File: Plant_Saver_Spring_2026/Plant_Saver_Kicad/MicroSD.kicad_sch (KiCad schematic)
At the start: 7 parts, among them J3 DM3D-SF

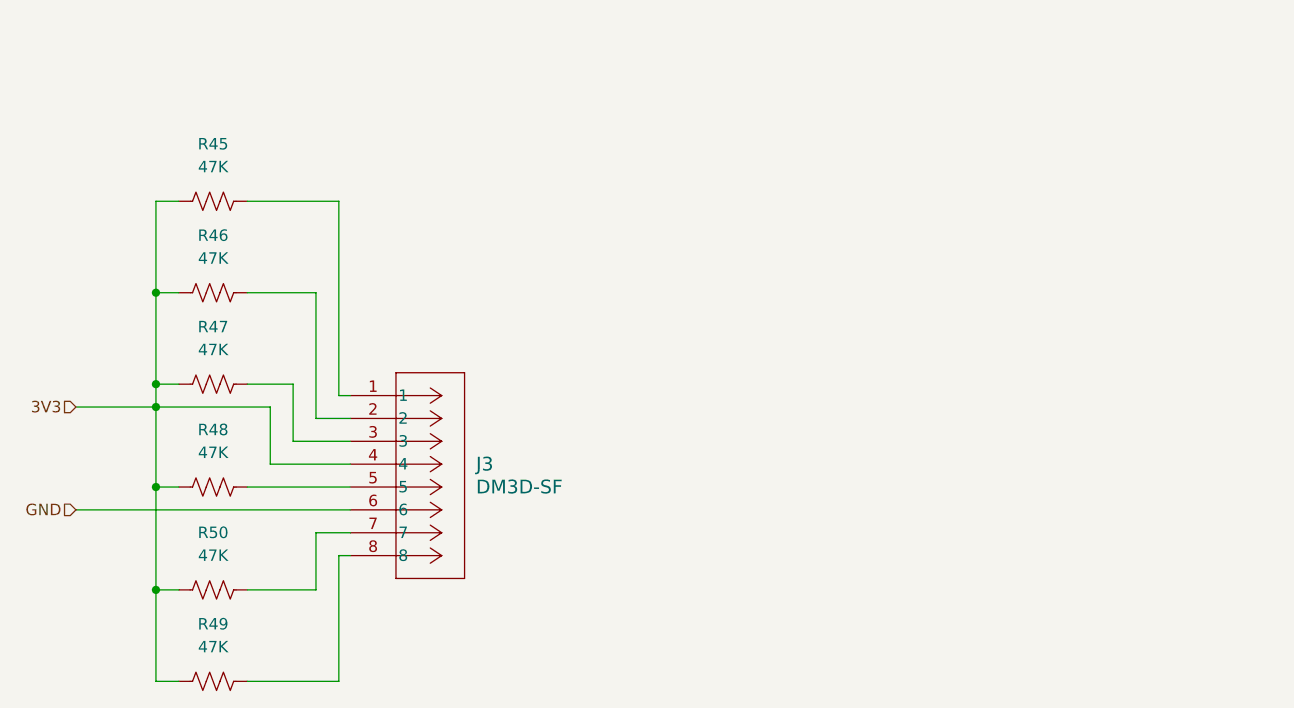
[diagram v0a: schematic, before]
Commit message: Micro-SD subsheet
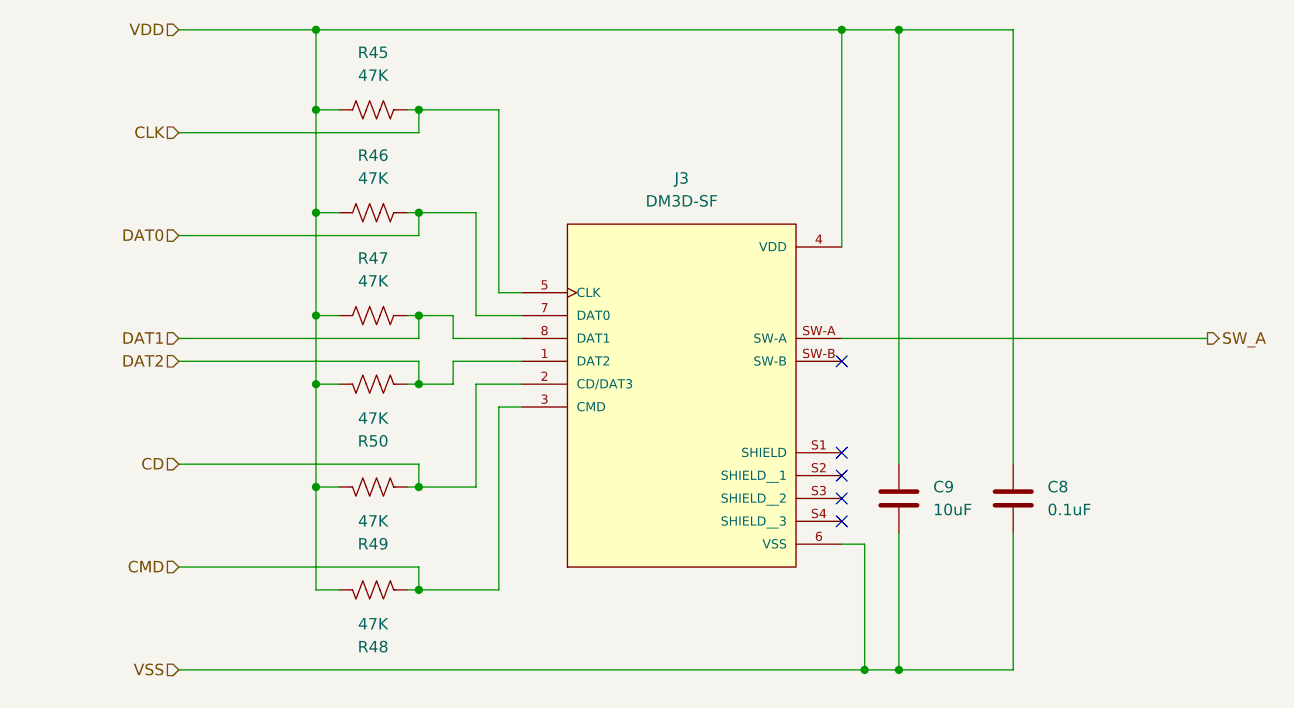
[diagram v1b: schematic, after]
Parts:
- added C8: 0.1uF, Capacitor_SMD:C_1206_3216Metric_Pad1.33x1.80mm_HandSolder, symbol Device:C
- added C9: 10uF, Capacitor_SMD:C_1206_3216Metric_Pad1.33x1.80mm_HandSolder, symbol Device:C
- J3: footprint DM3D_SF:CONN8_DM3D-SF_HIR -> DM3D_SF:HRS_DM3D-SF; MANUFACTURER (none) -> Hirose; MAXIMUM_PACKAGE_HEIGHT (none) -> 1.55mm; PARTREV (none) -> 2017.1; STANDARD (none) -> Manufacturer Recommendations
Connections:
- net CLK: now reaches J3.5 (CLK)
- net CLK: now also R45.2; no longer R48.2
- net DAT0: now reaches J3.7 (DAT0)
- net DAT0: now also R46.2; no longer R50.2
- net DAT2: now reaches J3.1 (DAT2)
- net DAT2: now also R50.2; no longer R45.2
- net CD: now reaches J3.2 (CD/DAT3)
- net CD: now also R49.2; no longer R46.2
- net CMD: now reaches J3.3 (CMD)
- net CMD: now also R48.2; no longer R47.2
- net DAT1: now reaches J3.8 (DAT1)
- net DAT1: now also R47.2; no longer R49.2
- net 3V3 renamed VDD
- net VDD: now also C8.1, C9.1
- net GND renamed VSS
- net VSS: now also C8.2, C9.2
- new net SW_A: J3.SW-A
- no-connect marks 0 -> 5
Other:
- moved on the sheet: R45, R46, R47

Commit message: Misc. changes
Updated peripheral power switch, UI board connections
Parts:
- R45, R46, R47, R48, R49, R50: value 47K -> 10K
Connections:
- net VDD is gone; now on net CD: C8.1, C9.1, J3.4 (VDD), R45.1, R46.1, R47.1, R48.1, R49.1, R50.1
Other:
- moved on the sheet: R48, R49, R50

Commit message: Started PCB
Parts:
- renumbered C8 to C10, J3 to J10, R45 to R18, R46 to R19, R47 to R20, R50 to R21, R49 to R22, R48 to R23
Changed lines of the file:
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@@
 		(dnp no)
 		(fields_autoplaced yes)
-		(property "Reference" "R48"
+		(property "Reference" "R23"
 			(at 116.84 109.22 90)
 			(effects
@@
 			(project "Plant_Saver_Kicad"
 				(path "/7f244634-d37a-4ff0-ba36-8027330ab1bd/bf3b52d9-1787-462a-86c6-de9a695c648b"
-					(reference "R48")
+					(reference "R23")
 					(unit 1)
 				)
@@
 		(dnp no)
 		(fields_autoplaced yes)
-		(property "Reference" "R50"
+		(property "Reference" "R21"
 			(at 116.84 88.9 90)
 			(effects
@@
 			(project "Plant_Saver_Kicad"
 				(path "/7f244634-d37a-4ff0-ba36-8027330ab1bd/bf3b52d9-1787-462a-86c6-de9a695c648b"
-					(reference "R50")
+					(reference "R21")
 					(unit 1)
 				)
@@
 		(dnp no)
 		(fields_autoplaced yes)
-		(property "Reference" "R47"
+		(property "Reference" "R20"
 			(at 116.84 77.47 90)
 			(effects
@@
 			(project "Plant_Saver_Kicad"
 				(path "/7f244634-d37a-4ff0-ba36-8027330ab1bd/bf3b52d9-1787-462a-86c6-de9a695c648b"
-					(reference "R47")
+					(reference "R20")
 					(unit 1)
 				)
@@
 		(dnp no)
 		(fields_autoplaced yes)
-		(property "Reference" "R45"
+		(property "Reference" "R18"
 			(at 116.84 54.61 90)
 			(effects
@@
 			(project ""
 				(path "/7f244634-d37a-4ff0-ba36-8027330ab1bd/bf3b52d9-1787-462a-86c6-de9a695c648b"
-					(reference "R45")
+					(reference "R18")
 					(unit 1)
 				)
@@
 		(dnp no)
 		(fields_autoplaced yes)
-		(property "Reference" "J3"
+		(property "Reference" "J10"
 			(at 151.13 68.58 0)
 			(effects
@@
 			(project ""
 				(path "/7f244634-d37a-4ff0-ba36-8027330ab1bd/bf3b52d9-1787-462a-86c6-de9a695c648b"
-					(reference "J3")
+					(reference "J10")
 					(unit 1)
 				)
@@
 		(dnp no)
 		(fields_autoplaced yes)
-		(property "Reference" "C8"
+		(property "Reference" "C10"
 			(at 191.77 102.8699 0)
 			(effects
@@
 			(project ""
 				(path "/7f244634-d37a-4ff0-ba36-8027330ab1bd/bf3b52d9-1787-462a-86c6-de9a695c648b"
-					(reference "C8")
+					(reference "C10")
 					(unit 1)
 				)
@@
 		(dnp no)
 		(fields_autoplaced yes)
-		(property "Reference" "R46"
+		(property "Reference" "R19"
 			(at 116.84 66.04 90)
 			(effects
@@
 			(project "Plant_Saver_Kicad"
 				(path "/7f244634-d37a-4ff0-ba36-8027330ab1bd/bf3b52d9-1787-462a-86c6-de9a695c648b"
-					(reference "R46")
+					(reference "R19")
 					(unit 1)
 				)
@@
 		(dnp no)
 		(fields_autoplaced yes)
-		(property "Reference" "R49"
+		(property "Reference" "R22"
 			(at 116.84 99.06 90)
 			(effects
@@
 			(project "Plant_Saver_Kicad"
 				(path "/7f244634-d37a-4ff0-ba36-8027330ab1bd/bf3b52d9-1787-462a-86c6-de9a695c648b"
-					(reference "R49")
-					(unit 1)
-				)
+					(reference "R22")
+					(unit 1)
+				)

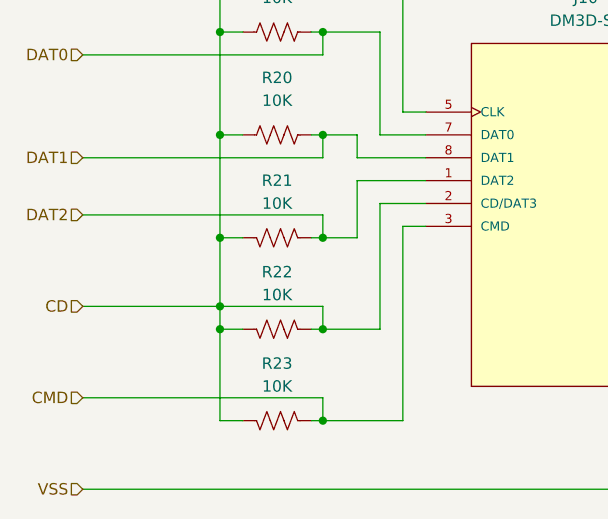
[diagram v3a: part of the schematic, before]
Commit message: Refined PCB layout
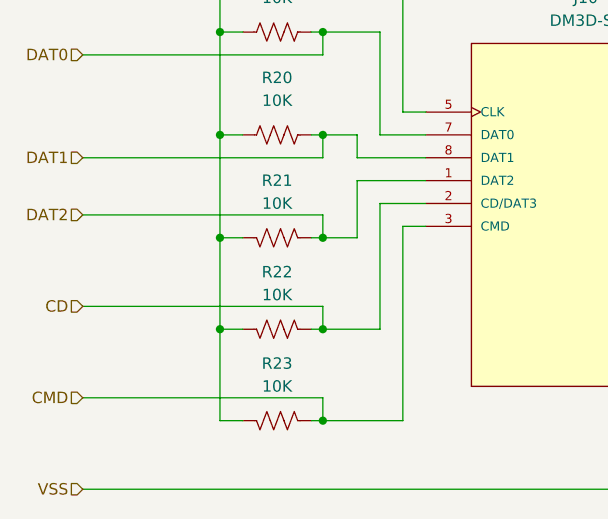
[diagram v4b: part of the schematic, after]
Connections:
- net CD: no longer C10.1, C9.1, J10.4 (VDD), R18.1, R19.1, R20.1, R21.1, R22.1, R23.1
- new net VDD: C10.1, C9.1, J10.4 (VDD), R18.1, R19.1, R20.1, R21.1, R22.1, R23.1
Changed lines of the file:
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@@
-	)
-	(junction
-		(at 110.49 102.87)
-		(diameter 0)
-		(color 0 0 0 0)
 	)
 	(junction
@@
 	(wire
 		(pts
-			(xy 95.25 102.87) (xy 110.49 102.87)
-		)
-		(stroke
-			(width 0)
-			(type default)
-		)
-	)
-	(wire
-		(pts
 			(xy 120.65 83.82) (xy 121.92 83.82)
 		)
@@
 	(wire
 		(pts
-			(xy 110.49 95.25) (xy 110.49 102.87)
-		)
-		(stroke
-			(width 0)
-			(type default)
-		)
-	)
-	(wire
-		(pts
 			(xy 121.92 105.41) (xy 121.92 102.87)
 		)
@@
 	(wire
 		(pts
-			(xy 110.49 105.41) (xy 110.49 102.87)
+			(xy 110.49 95.25) (xy 110.49 105.41)
 		)
 		(stroke
@@
 	(wire
 		(pts
-			(xy 110.49 102.87) (xy 121.92 102.87)
-		)
-		(stroke
+			(xy 95.25 102.87) (xy 121.92 102.87)
+		)
+		(stroke

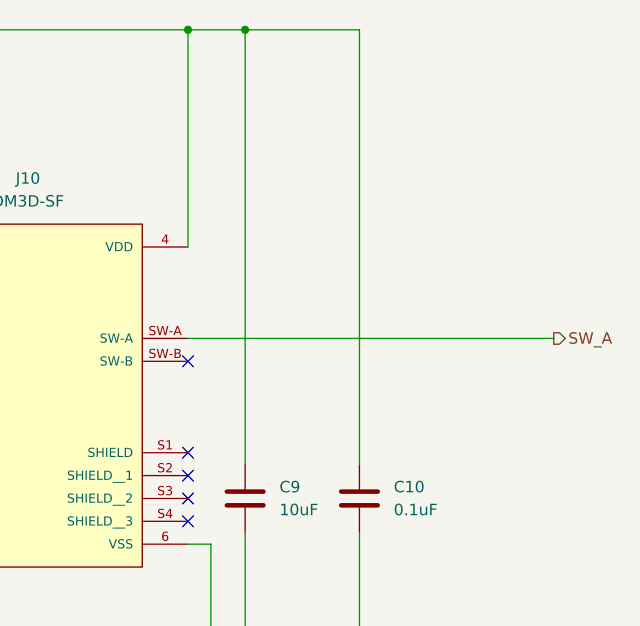
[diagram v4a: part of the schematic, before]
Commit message: Nearly finished routing
uSD and two I2C connectors remaining.
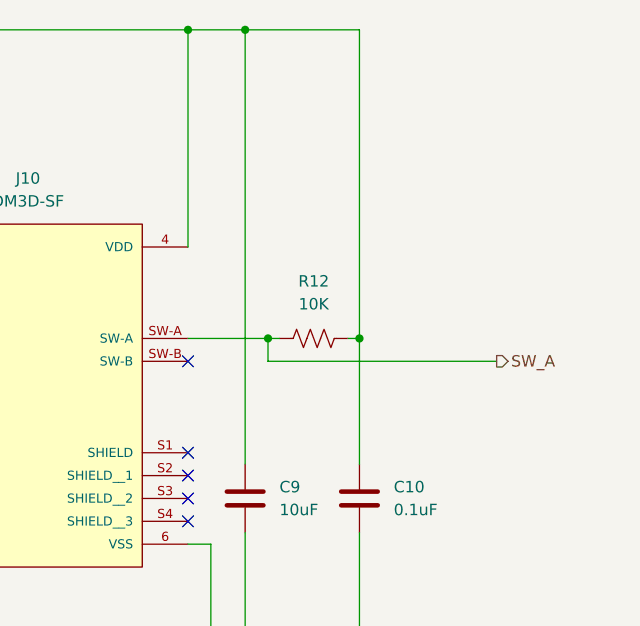
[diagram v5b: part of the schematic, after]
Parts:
- added R12: 10K, Resistor_SMD:R_1206_3216Metric_Pad1.30x1.75mm_HandSolder, symbol Device:R_US
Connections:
- net SW_A: now also R12.1
- net VDD: now also R12.2
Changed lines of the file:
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@@
+	)
+	(junction
+		(at 177.8 86.36)
+		(diameter 0)
+		(color 0 0 0 0)
 	)
 	(junction
@@
 	)
 	(junction
+		(at 187.96 86.36)
+		(diameter 0)
+		(color 0 0 0 0)
+	)
+	(junction
 		(at 110.49 72.39)
 		(diameter 0)
@@
 	(wire
 		(pts
+			(xy 177.8 88.9) (xy 177.8 86.36)
+		)
+		(stroke
+			(width 0)
+			(type default)
+		)
+	)
+	(wire
+		(pts
 			(xy 120.65 95.25) (xy 121.92 95.25)
 		)
@@
 	(wire
 		(pts
+			(xy 186.69 86.36) (xy 187.96 86.36)
+		)
+		(stroke
+			(width 0)
+			(type default)
+		)
+	)
+	(wire
+		(pts
 			(xy 125.73 86.36) (xy 133.35 86.36)
 		)
@@
 	(wire
 		(pts
-			(xy 168.91 86.36) (xy 209.55 86.36)
-		)
-		(stroke
-			(width 0)
-			(type default)
-		)
-	)
-	(wire
-		(pts
 			(xy 128.27 72.39) (xy 128.27 83.82)
 		)
@@
 	(wire
 		(pts
+			(xy 203.2 88.9) (xy 177.8 88.9)
+		)
+		(stroke
+			(width 0)
+			(type default)
+		)
+	)
+	(wire
+		(pts
 			(xy 175.26 123.19) (xy 171.45 123.19)
 		)
@@
 	(wire
 		(pts
+			(xy 187.96 86.36) (xy 187.96 100.33)
+		)
+		(stroke
+			(width 0)
+			(type default)
+		)
+	)
+	(wire
+		(pts
 			(xy 95.25 102.87) (xy 121.92 102.87)
 		)
@@
 	(wire
 		(pts
+			(xy 168.91 86.36) (xy 177.8 86.36)
+		)
+		(stroke
+			(width 0)
+			(type default)
+		)
+	)
+	(wire
+		(pts
 			(xy 110.49 60.96) (xy 110.49 72.39)
 		)
@@
 	(wire
 		(pts
-			(xy 187.96 52.07) (xy 187.96 100.33)
+			(xy 187.96 52.07) (xy 187.96 86.36)
 		)
 		(stroke
@@
 		(pts
 			(xy 121.92 115.57) (xy 130.81 115.57)
+		)
+		(stroke
+			(width 0)
+			(type default)
+		)
+	)
+	(wire
+		(pts
+			(xy 177.8 86.36) (xy 179.07 86.36)
 		)
 		(stroke
@@
 	(hierarchical_label "SW_A"
 		(shape output)
-		(at 209.55 86.36 0)
+		(at 203.2 88.9 0)
 		(effects
 			(font
@@
 					(unit 1)
 				)
+			)
+		)
+	)
+	(symbol
+		(lib_id "Device:R_US")
+		(at 182.88 86.36 90)
+		(unit 1)
+		(exclude_from_sim no)
+		(in_bom yes)
+		(on_board yes)
+		(dnp no)
+		(property "Reference" "R12"
+			(at 182.88 80.01 90)
+			(effects
+				(font
+					(size 1.27 1.27)
+				)
+			)
+		)
+		(property "Value" "10K"
+			(at 182.88 82.55 90)
+			(effects
+				(font
+					(size 1.27 1.27)
+				)
+			)
+		)
+		(property "Footprint" "Resistor_SMD:R_1206_3216Metric_Pad1.30x1.75mm_HandSolder"
+			(at 183.134 85.344 90)
+			(effects
+				(font
+					(size 1.27 1.27)
+				)
+				(hide yes)
+			)
+		)
+		(property "Datasheet" "~"
+			(at 182.88 86.36 0)
+			(effects
+				(font
+					(size 1.27 1.27)
+				)
+				(hide yes)
+			)
+		)
+		(property "Description" "Resistor, US symbol"
+			(at 182.88 86.36 0)
+			(effects
+				(font
+					(size 1.27 1.27)
+				)
+				(hide yes)
+			)
+		)
+		(pin "1"
+		)
+		(pin "2"
+		)
+		(instances
+			(project "Plant_Saver_Kicad"
+				(path "/7f244634-d37a-4ff0-ba36-8027330ab1bd/bf3b52d9-1787-462a-86c6-de9a695c648b"
+					(reference "R12")
+					(unit 1)
+				)

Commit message: PCB Pre-Check complete
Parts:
- renumbered J10 to J11, R18 to R19, R19 to R20, R20 to R21, R21 to R22, R22 to R23, R23 to R24, R12 to R25
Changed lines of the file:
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@@
 		(dnp no)
 		(fields_autoplaced yes)
-		(property "Reference" "R23"
+		(property "Reference" "R24"
 			(at 116.84 109.22 90)
 			(effects
@@
 			(project "Plant_Saver_Kicad"
 				(path "/7f244634-d37a-4ff0-ba36-8027330ab1bd/bf3b52d9-1787-462a-86c6-de9a695c648b"
-					(reference "R23")
+					(reference "R24")
 					(unit 1)
 				)
@@
 		(dnp no)
 		(fields_autoplaced yes)
-		(property "Reference" "R21"
+		(property "Reference" "R22"
 			(at 116.84 88.9 90)
 			(effects
@@
 			(project "Plant_Saver_Kicad"
 				(path "/7f244634-d37a-4ff0-ba36-8027330ab1bd/bf3b52d9-1787-462a-86c6-de9a695c648b"
-					(reference "R21")
+					(reference "R22")
 					(unit 1)
 				)
@@
 		(dnp no)
 		(fields_autoplaced yes)
-		(property "Reference" "R20"
+		(property "Reference" "R21"
 			(at 116.84 77.47 90)
 			(effects
@@
 			(project "Plant_Saver_Kicad"
 				(path "/7f244634-d37a-4ff0-ba36-8027330ab1bd/bf3b52d9-1787-462a-86c6-de9a695c648b"
-					(reference "R20")
+					(reference "R21")
 					(unit 1)
 				)
@@
 		(on_board yes)
 		(dnp no)
-		(property "Reference" "R12"
+		(property "Reference" "R25"
 			(at 182.88 80.01 90)
 			(effects
@@
 			(project "Plant_Saver_Kicad"
 				(path "/7f244634-d37a-4ff0-ba36-8027330ab1bd/bf3b52d9-1787-462a-86c6-de9a695c648b"
-					(reference "R12")
+					(reference "R25")
 					(unit 1)
 				)
@@
 		(dnp no)
 		(fields_autoplaced yes)
-		(property "Reference" "R18"
+		(property "Reference" "R19"
 			(at 116.84 54.61 90)
 			(effects
@@
 			(project ""
 				(path "/7f244634-d37a-4ff0-ba36-8027330ab1bd/bf3b52d9-1787-462a-86c6-de9a695c648b"
-					(reference "R18")
+					(reference "R19")
 					(unit 1)
 				)
@@
 		(dnp no)
 		(fields_autoplaced yes)
-		(property "Reference" "J10"
+		(property "Reference" "J11"
 			(at 151.13 68.58 0)
 			(effects
@@
 			(project ""
 				(path "/7f244634-d37a-4ff0-ba36-8027330ab1bd/bf3b52d9-1787-462a-86c6-de9a695c648b"
-					(reference "J10")
+					(reference "J11")
 					(unit 1)
 				)
@@
 		(dnp no)
 		(fields_autoplaced yes)
-		(property "Reference" "R19"
+		(property "Reference" "R20"
 			(at 116.84 66.04 90)
 			(effects
@@
 			(project "Plant_Saver_Kicad"
 				(path "/7f244634-d37a-4ff0-ba36-8027330ab1bd/bf3b52d9-1787-462a-86c6-de9a695c648b"
-					(reference "R19")
+					(reference "R20")
 					(unit 1)
 				)
@@
 		(dnp no)
 		(fields_autoplaced yes)
-		(property "Reference" "R22"
+		(property "Reference" "R23"
 			(at 116.84 99.06 90)
 			(effects
@@
 			(project "Plant_Saver_Kicad"
 				(path "/7f244634-d37a-4ff0-ba36-8027330ab1bd/bf3b52d9-1787-462a-86c6-de9a695c648b"
-					(reference "R22")
-					(unit 1)
-				)
+					(reference "R23")
+					(unit 1)
+				)
